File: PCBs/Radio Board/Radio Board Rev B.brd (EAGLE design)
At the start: 160 x 100 mm, 5 parts, among them T2 AD590KRZ

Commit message: Changed Li Tx/Rx pins
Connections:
- net LITHIUM_RX_UART: now also U$2.P$29; no longer U$2.P$37
- net LITHIUM_TX_UART: now also U$2.P$31; no longer U$2.P$39
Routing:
- net LITHIUM_TX_UART: track 17.7 -> 25.9 mm
- net LITHIUM_RX_UART: track 17.4 -> 25.4 mm
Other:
- board size 160 x 100 mm -> 95.2 x 90.5 mm
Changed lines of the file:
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@@
 <?xml version="1.0" encoding="utf-8"?>
 <!DOCTYPE eagle SYSTEM "eagle.dtd">
-<eagle version="9.0.1">
+<eagle version="9.1.0">
 <drawing>
 <settings>
@@
 <board>
 <plain>
-<wire x1="0" y1="0" x2="160" y2="0" width="0" layer="20"/>
-<wire x1="160" y1="0" x2="160" y2="100" width="0" layer="20"/>
-<wire x1="160" y1="100" x2="0" y2="100" width="0" layer="20"/>
-<wire x1="0" y1="100" x2="0" y2="0" width="0" layer="20"/>
+<wire x1="1.905" y1="1.905" x2="97.135" y2="1.905" width="0" layer="20"/>
+<wire x1="97.135" y1="1.905" x2="97.135" y2="92.38" width="0" layer="20"/>
+<wire x1="97.135" y1="92.38" x2="1.905" y2="92.38" width="0" layer="20"/>
+<wire x1="1.905" y1="92.38" x2="1.905" y2="1.905" width="0" layer="20"/>
 </plain>
 <attributes>
@@
 <param name="checkStop" value="0"/>
 <param name="checkValues" value="0"/>
+<param name="checkNames" value="1"/>
+<param name="checkWireStubs" value="1"/>
+<param name="checkPolygonWidth" value="0"/>
 <param name="useDiameter" value="13"/>
 <param name="maxErrors" value="50"/>
@@
 <via x="46.355" y="55.88" extent="1-16" drill="4.999990625"/>
 <polygon width="0.1524" layer="16">
-<vertex x="1.27" y="93.98"/>
-<vertex x="97.79" y="93.98"/>
-<vertex x="97.79" y="1.27"/>
-<vertex x="1.905" y="1.27"/>
-<vertex x="1.27" y="1.905"/>
+<vertex x="3.175" y="91.44"/>
+<vertex x="95.25" y="91.44"/>
+<vertex x="95.25" y="3.175"/>
+<vertex x="3.175" y="3.175"/>
 </polygon>
 <wire x1="35.56" y1="31.242" x2="35.582" y2="31.22" width="0.508" layer="1"/>
@@
 <contactref element="U$1" pad="3.3V"/>
 <wire x1="92.31121875" y1="58.42" x2="91.04121875" y2="57.15" width="0.1524" layer="1"/>
-<wire x1="91.04121875" y1="57.15" x2="83.185" y2="57.15" width="0.1524" layer="1"/>
-<wire x1="83.185" y1="57.15" x2="80.645" y2="54.61" width="0.1524" layer="1"/>
+<wire x1="83.185" y1="57.15" x2="91.04121875" y2="57.15" width="0.1524" layer="1"/>
 <contactref element="C2" pad="1"/>
 <wire x1="74.93" y1="34.478" x2="70.712" y2="34.478" width="0.635" layer="1"/>
 <wire x1="70.712" y1="34.478" x2="70.7" y2="34.49" width="0.635" layer="1"/>
-<wire x1="80.645" y1="54.61" x2="80.645" y2="40.193" width="0.1524" layer="1"/>
-<wire x1="80.645" y1="40.193" x2="74.93" y2="34.478" width="0.1524" layer="1"/>
+<wire x1="74.93" y1="34.478" x2="74.93" y2="48.895" width="0.1524" layer="1"/>
+<wire x1="74.93" y1="48.895" x2="83.185" y2="57.15" width="0.1524" layer="1"/>
 </signal>
 <signal name="LITHIUM_TX_UART">
 <contactref element="U$1" pad="TX_UART"/>
-<contactref element="U$2" pad="P$39"/>
 <wire x1="70.7" y1="21.41" x2="70.88" y2="21.59" width="0.1524" layer="1"/>
 <wire x1="70.88" y1="21.59" x2="72.39" y2="21.59" width="0.1524" layer="1"/>
-<wire x1="72.39" y1="21.59" x2="81.28" y2="30.48" width="0.1524" layer="1"/>
-<wire x1="81.28" y1="30.48" x2="84.69121875" y2="30.48" width="0.1524" layer="1"/>
+<contactref element="U$2" pad="P$31"/>
+<wire x1="83.185" y1="39.13378125" x2="84.69121875" y2="40.64" width="0.1524" layer="1"/>
+<wire x1="72.39" y1="21.59" x2="83.185" y2="32.385" width="0.1524" layer="1"/>
+<wire x1="83.185" y1="32.385" x2="83.185" y2="39.13378125" width="0.1524" layer="1"/>
 </signal>
 <signal name="LITHIUM_RX_UART">
 <contactref element="U$1" pad="RX_UART"/>
-<contactref element="U$2" pad="P$37"/>
 <wire x1="70.7" y1="24.68" x2="70.785" y2="24.765" width="0.1524" layer="1"/>
 <wire x1="70.785" y1="24.765" x2="72.39" y2="24.765" width="0.1524" layer="1"/>
-<wire x1="72.39" y1="24.765" x2="80.645" y2="33.02" width="0.1524" layer="1"/>
-<wire x1="80.645" y1="33.02" x2="84.69121875" y2="33.02" width="0.1524" layer="1"/>
+<contactref element="U$2" pad="P$29"/>
+<wire x1="81.915" y1="34.29" x2="81.915" y2="40.64" width="0.1524" layer="1"/>
+<wire x1="81.915" y1="40.64" x2="84.455" y2="43.18" width="0.1524" layer="1"/>
+<wire x1="84.455" y1="43.18" x2="84.69121875" y2="43.18" width="0.1524" layer="1"/>
+<wire x1="72.39" y1="24.765" x2="81.915" y2="34.29" width="0.1524" layer="1"/>
 </signal>
 <signal name="SW5">
@@
 </signal>
 </signals>
+<mfgpreviewcolors>
+<mfgpreviewcolor name="soldermaskcolor" color="0xC8008000"/>
+<mfgpreviewcolor name="silkscreencolor" color="0xFFFEFEFE"/>
+<mfgpreviewcolor name="backgroundcolor" color="0xFF282828"/>
+<mfgpreviewcolor name="coppercolor" color="0xFFFFBF00"/>
+<mfgpreviewcolor name="substratecolor" color="0xFF786E46"/>
+</mfgpreviewcolors>
 </board>
 </drawing>

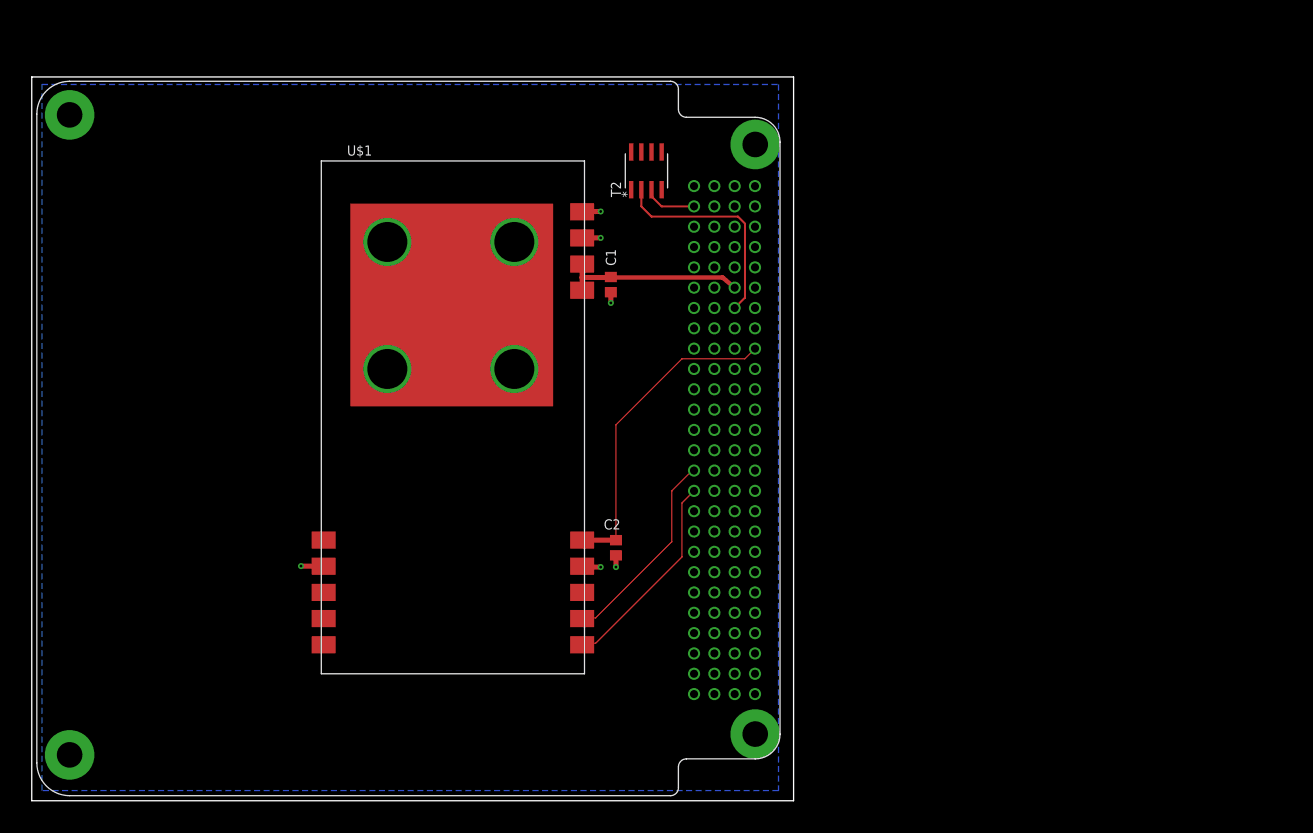
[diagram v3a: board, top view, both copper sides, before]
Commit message: Remove temp sensor, tweak trace width
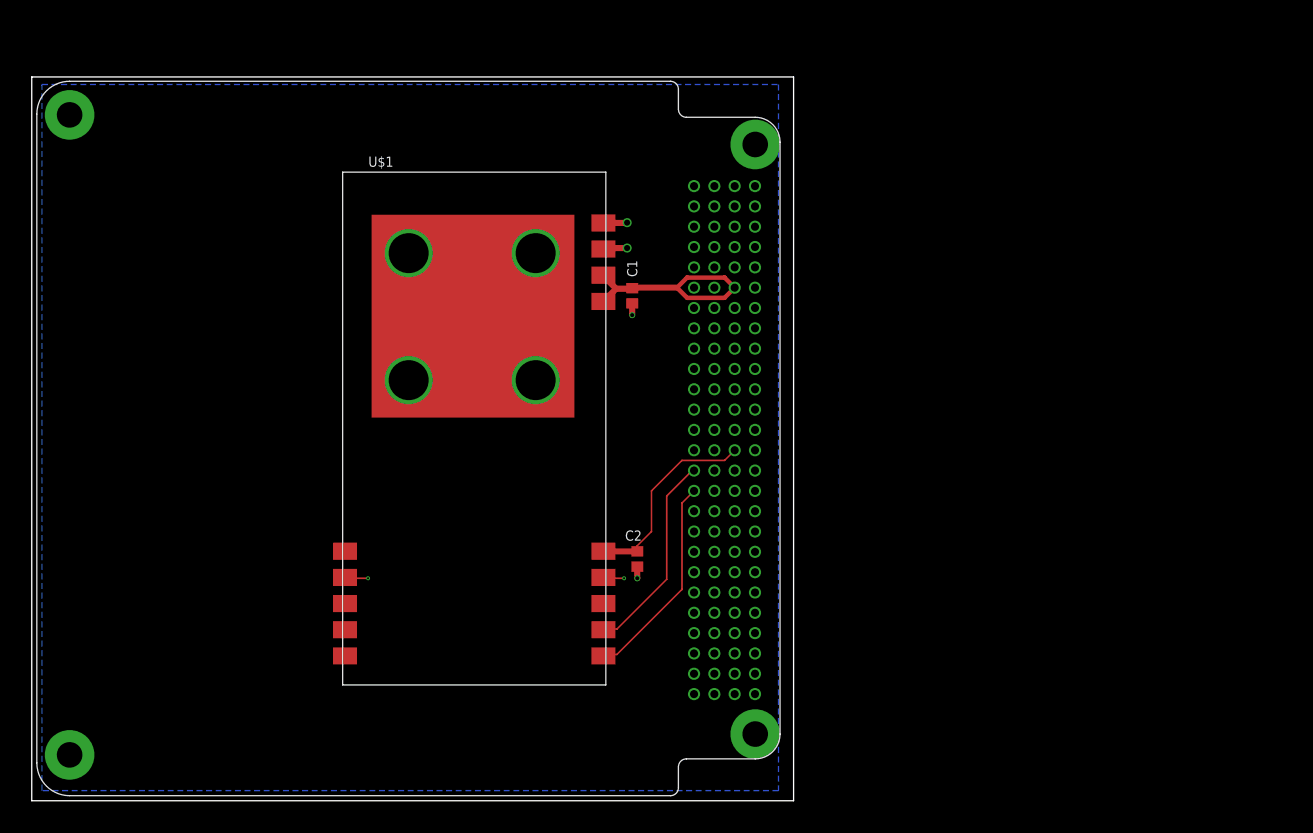
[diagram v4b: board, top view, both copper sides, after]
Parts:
- removed T2: AD590KRZ, AD590KRZ:R_8
- moved C1 3.01 mm to (77.0, 65.0)
- moved U$1 3.01 mm to (40.8, 16.4)
- moved C2 3.01 mm to (77.6, 32.1)
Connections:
- removed net N$1: T2.3, U$2.P$3
- removed net SW8: C2.1, U$1.3.3V, U$2.P$70
- new net 3V3: C2.1, U$1.3.3V, U$2.P$79
- net SW5: no longer T2.2
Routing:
- net SW8: track 40.0 -> 0.00 mm
- net SW5: track 27.0 -> 0.00 mm
- net 3V3: track 0.00 -> 25.0 mm
- net N$1: track 6.66 -> 0.00 mm
- net SW3: track 22.9 -> 28.8 mm
- net GND: track 12.8 -> 14.5 mm

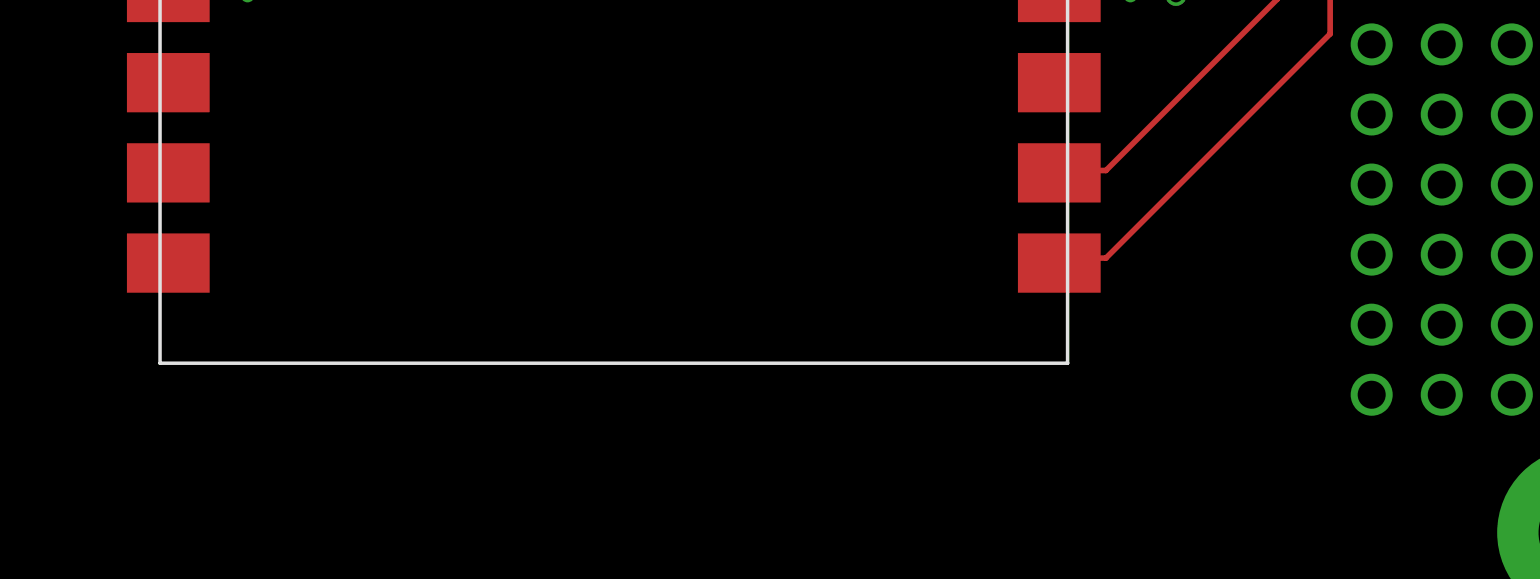
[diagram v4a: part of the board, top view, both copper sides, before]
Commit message: Added Lithium OA system reset
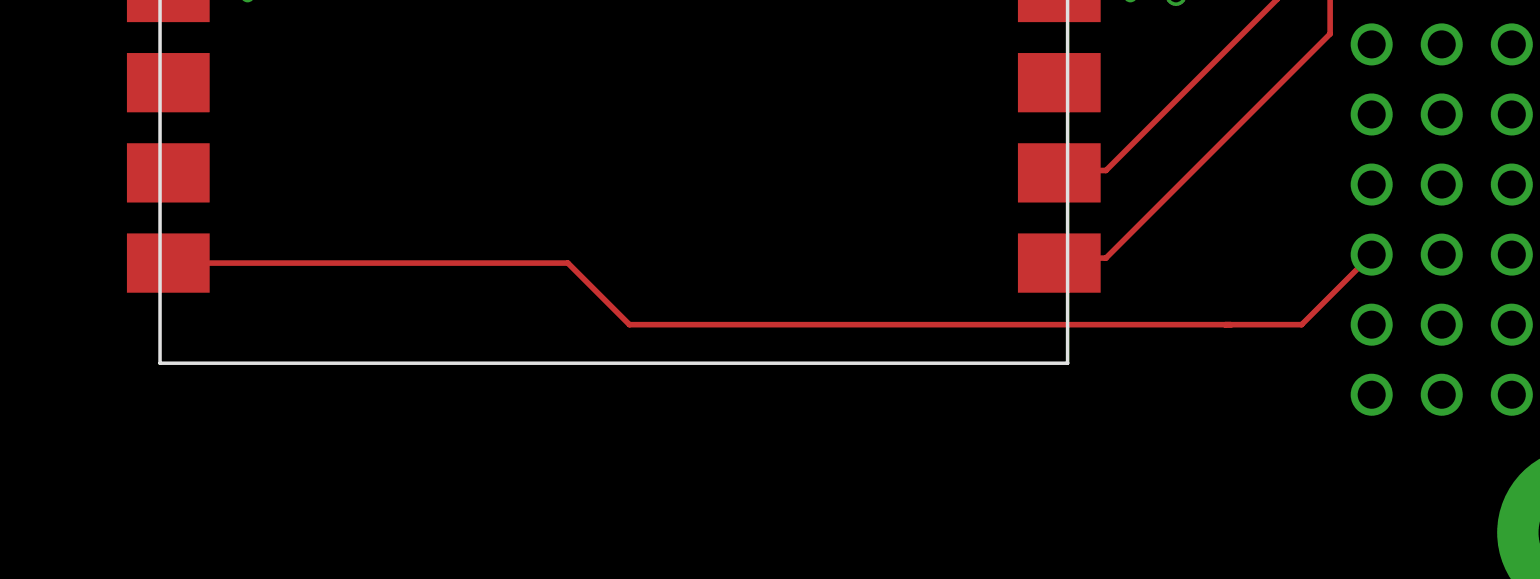
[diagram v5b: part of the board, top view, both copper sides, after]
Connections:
- removed net SW5: U$2.P$65
- new net OA_RESET: U$1.CONFIG1, U$2.P$47
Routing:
- net OA_RESET: track 0.00 -> 45.8 mm
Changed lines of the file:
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@@
 <wire x1="75.057" y1="23.368" x2="81.28" y2="29.591" width="0.2032" layer="1"/>
-</signal>
-<signal name="SW5">
-<contactref element="U$2" pad="P$65"/>
 </signal>
 <signal name="3V3">
@@
 <wire x1="73.379" y1="33.081" x2="73.367" y2="33.093" width="0.604" layer="1"/>
 </signal>
+<signal name="OA_RESET">
+<contactref element="U$1" pad="CONFIG1"/>
+<wire x1="41.067" y1="20.013" x2="55.552" y2="20.013" width="0.2032" layer="1"/>
+<wire x1="55.552" y1="20.013" x2="57.785" y2="17.78" width="0.2032" layer="1"/>
+<wire x1="57.785" y1="17.78" x2="79.375" y2="17.78" width="0.2032" layer="1"/>
+<contactref element="U$2" pad="P$47"/>
+<wire x1="79.375" y1="17.78" x2="79.61121875" y2="17.78" width="0.2032" layer="1"/>
+<wire x1="79.375" y1="17.78" x2="82.15121875" y2="17.78" width="0.2032" layer="1"/>
+<wire x1="82.15121875" y1="17.78" x2="84.69121875" y2="20.32" width="0.2032" layer="1"/>
+</signal>
 </signals>
 <mfgpreviewcolors>
@@
 <mfgpreviewcolor name="substratecolor" color="0xFF786E46"/>
 </mfgpreviewcolors>
+<errors>
+</errors>
 </board>
 </drawing>

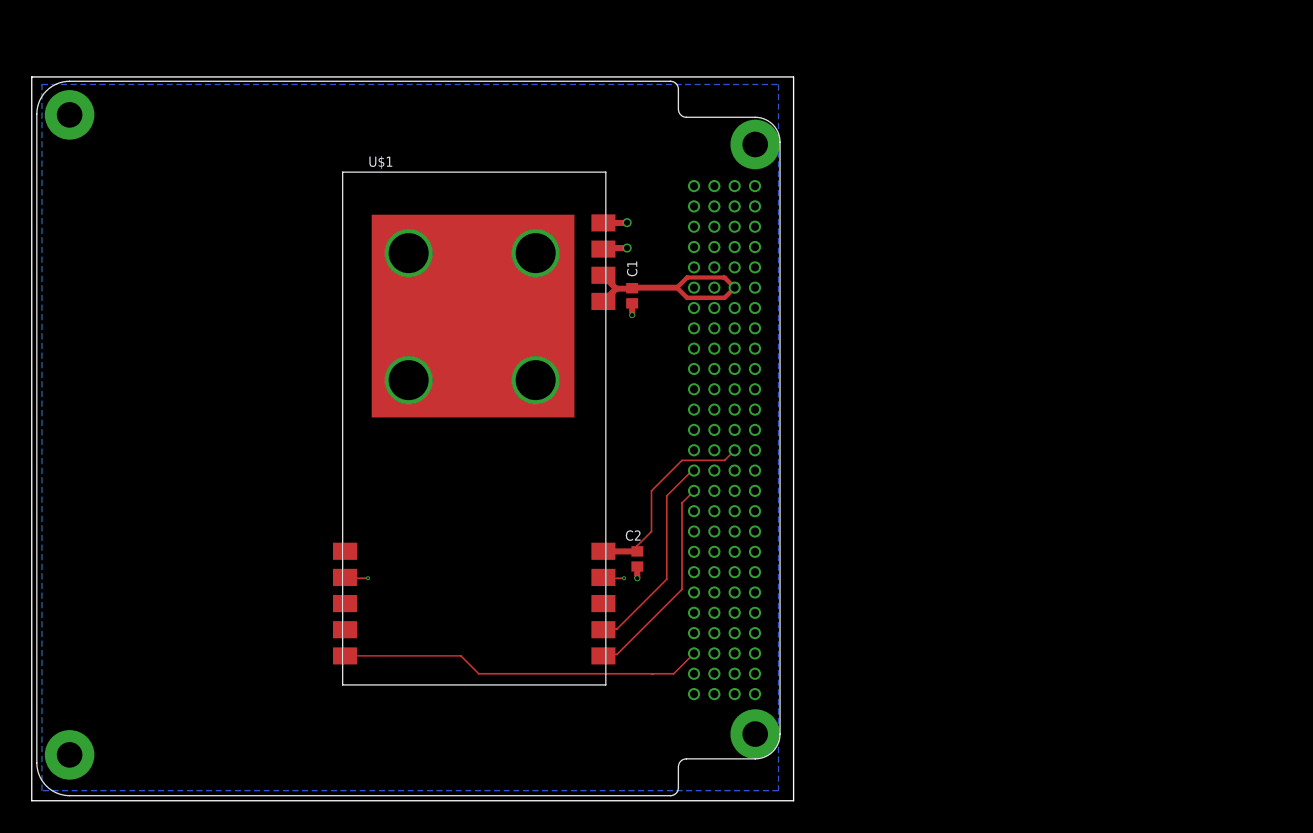
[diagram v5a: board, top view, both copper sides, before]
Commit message: Update radio board to use new library
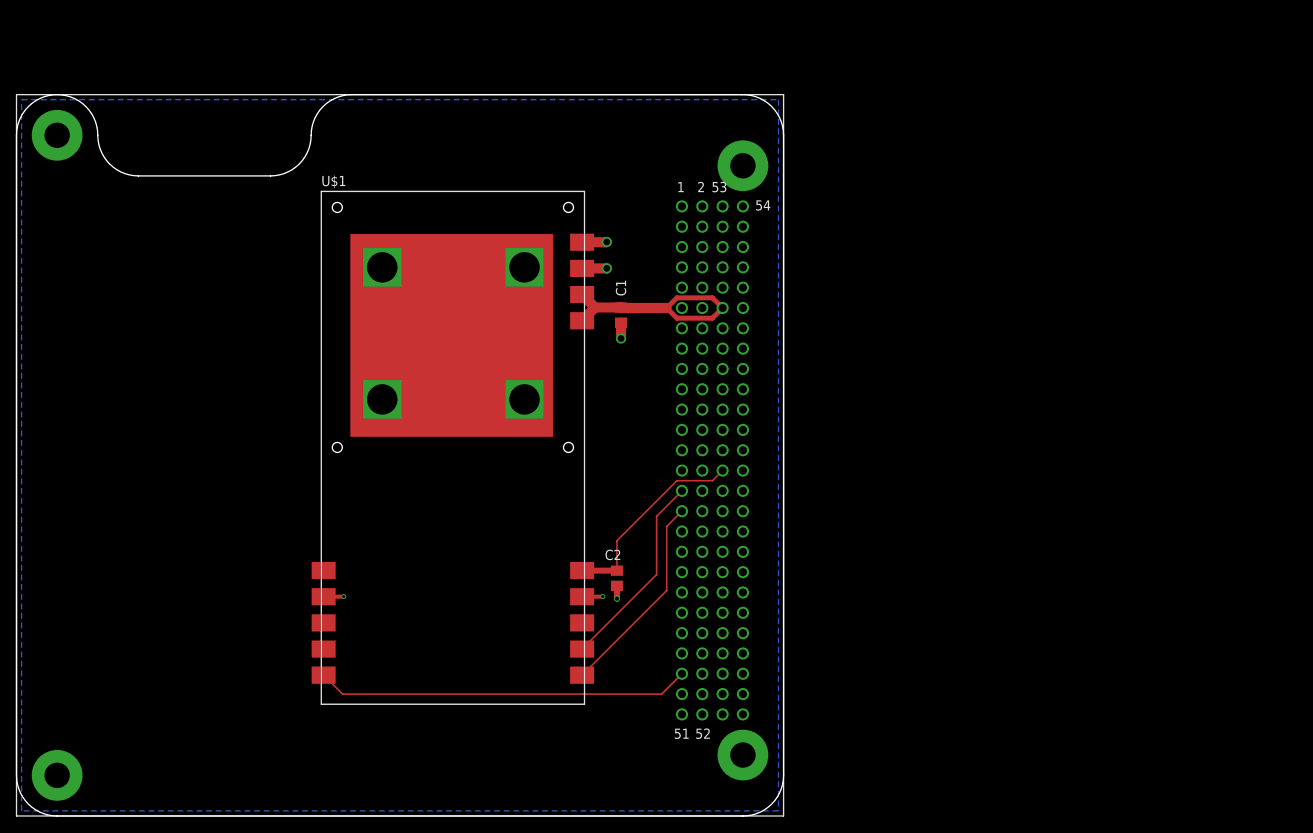
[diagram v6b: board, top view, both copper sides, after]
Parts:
- C1: value 1uF -> 10uF
- U$1: value LITHIUM -> LI-1
- U$2: value PC104 -> PC104_BOARD; device Cubesat:PC104 -> Cubesat:PC104_WITH_CSK_HEADER
- moved U$1 3.60 mm to (38.1, 14.0)
- moved U$2 3.59 mm to (0.00, 0.00)
- moved C2 3.50 mm to (75.1, 29.7)
- moved C1 2.79 mm to (75.6, 62.6)
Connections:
- removed net LITHIUM_RX_UART: U$1.RX_UART, U$2.P$29
- removed net LITHIUM_TX_UART: U$1.TX_UART, U$2.P$31
- new net LITHIUM_RX: U$1.RX_UART, U$2.29
- new net LITHIUM_TX: U$1.TX_UART, U$2.31
- net 3V3: now also U$2.79; no longer U$2.P$79
- net GND: now also U$2.100, U$2.61, U$2.66, U$2.69, U$2.73, U$2.74, U$2.81, U$2.82, U$2.84, U$2.99; no longer U$2.P$100, U$2.P$61, U$2.P$66, U$2.P$69, U$2.P$73, U$2.P$74, U$2.P$81, U$2.P$82, U$2.P$84, U$2.P$99
- net OA_RESET: now also U$2.47; no longer U$2.P$47
- net SW3: now also U$2.63; no longer U$2.P$63
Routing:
- net LITHIUM_TX_UART: track 26.2 -> 0.00 mm
- net LITHIUM_TX: track 0.00 -> 25.7 mm
- net LITHIUM_RX_UART: track 25.7 -> 0.00 mm
- net LITHIUM_RX: track 0.00 -> 24.9 mm
- net OA_RESET: track 45.8 -> 46.8 mm
- net SW3: track 28.8 -> 29.7 mm
- net GND: track 14.5 -> 14.8 mm, vias 10 -> 6
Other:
- board size 95.2 x 90.5 mm -> 95.9 x 90.2 mm
